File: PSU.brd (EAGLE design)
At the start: 100 x 50 mm, 20 parts, among them U1 MAX1896EUT+T

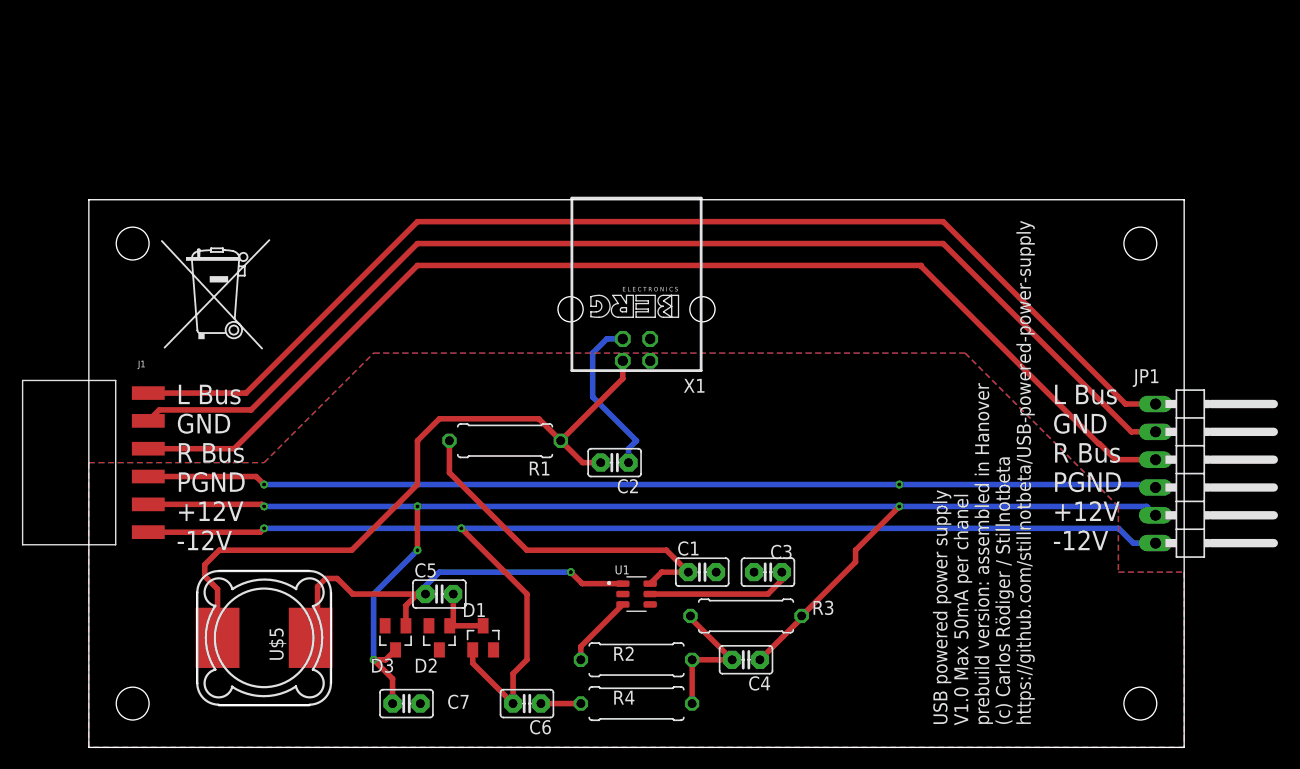
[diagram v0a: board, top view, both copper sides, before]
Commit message: V 1.1
These files have not been peer-reviewed and should NOT be manufactured.
Changes: Added rounded corners, added connection between U1 Pin 6 and Pin 4
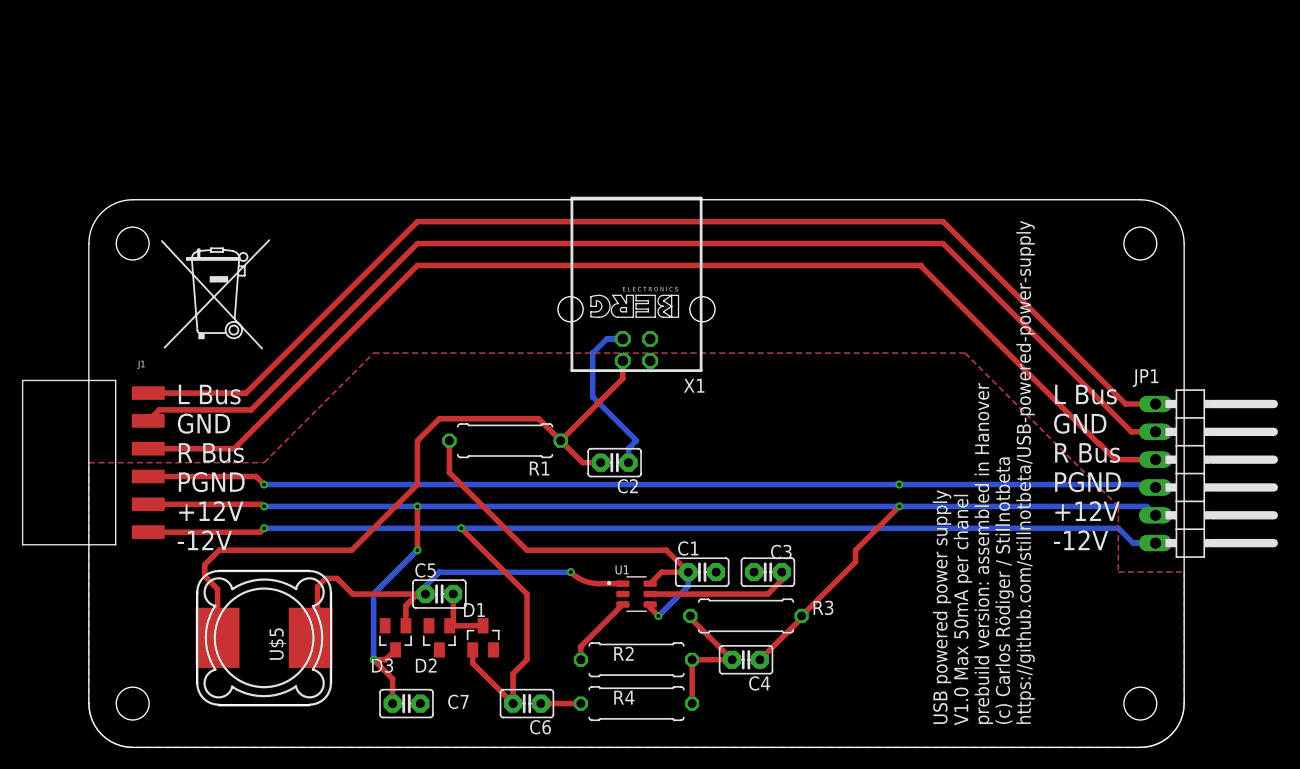
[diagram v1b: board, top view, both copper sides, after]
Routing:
- net N$1: track 32.4 -> 38.9 mm, vias 0 -> 1
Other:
- outline, holes or cut-outs redrawn
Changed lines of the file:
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@@
 <layer number="14" name="Route14" color="22" fill="1" visible="no" active="no"/>
 <layer number="15" name="Route15" color="23" fill="1" visible="no" active="no"/>
-<layer number="16" name="Bottom" color="1" fill="1" visible="no" active="yes"/>
+<layer number="16" name="Bottom" color="1" fill="1" visible="yes" active="yes"/>
 <layer number="17" name="Pads" color="2" fill="1" visible="yes" active="yes"/>
 <layer number="18" name="Vias" color="2" fill="1" visible="yes" active="yes"/>
@@
 <layer number="20" name="Dimension" color="24" fill="1" visible="yes" active="yes"/>
 <layer number="21" name="tPlace" color="7" fill="1" visible="yes" active="yes"/>
-<layer number="22" name="bPlace" color="7" fill="1" visible="no" active="yes"/>
+<layer number="22" name="bPlace" color="7" fill="1" visible="yes" active="yes"/>
 <layer number="23" name="tOrigins" color="15" fill="1" visible="yes" active="yes"/>
-<layer number="24" name="bOrigins" color="15" fill="1" visible="no" active="yes"/>
+<layer number="24" name="bOrigins" color="15" fill="1" visible="yes" active="yes"/>
 <layer number="25" name="tNames" color="7" fill="1" visible="yes" active="yes"/>
-<layer number="26" name="bNames" color="7" fill="1" visible="no" active="yes"/>
+<layer number="26" name="bNames" color="7" fill="1" visible="yes" active="yes"/>
 <layer number="27" name="tValues" color="7" fill="1" visible="no" active="yes"/>
 <layer number="28" name="bValues" color="7" fill="1" visible="no" active="yes"/>
@@
 <layer number="38" name="bTest" color="7" fill="1" visible="no" active="yes"/>
 <layer number="39" name="tKeepout" color="4" fill="11" visible="yes" active="yes"/>
-<layer number="40" name="bKeepout" color="1" fill="11" visible="no" active="yes"/>
+<layer number="40" name="bKeepout" color="1" fill="11" visible="yes" active="yes"/>
 <layer number="41" name="tRestrict" color="4" fill="10" visible="yes" active="yes"/>
-<layer number="42" name="bRestrict" color="1" fill="10" visible="no" active="yes"/>
+<layer number="42" name="bRestrict" color="1" fill="10" visible="yes" active="yes"/>
 <layer number="43" name="vRestrict" color="2" fill="10" visible="no" active="yes"/>
 <layer number="44" name="Drills" color="7" fill="1" visible="no" active="yes"/>
@@
 <layer number="50" name="dxf" color="7" fill="1" visible="no" active="no"/>
 <layer number="51" name="tDocu" color="7" fill="1" visible="yes" active="yes"/>
-<layer number="52" name="bDocu" color="7" fill="1" visible="no" active="yes"/>
+<layer number="52" name="bDocu" color="7" fill="1" visible="yes" active="yes"/>
 <layer number="53" name="tGND_GNDA" color="7" fill="9" visible="no" active="no"/>
 <layer number="54" name="bGND_GNDA" color="1" fill="9" visible="no" active="no"/>
@@
 <layer number="116" name="Patch_BOT" color="9" fill="4" visible="no" active="yes"/>
 <layer number="118" name="Rect_Pads" color="7" fill="1" visible="no" active="no"/>
-<layer number="121" name="_tsilk" color="7" fill="1" visible="yes" active="yes"/>
+<layer number="121" name="_tsilk" color="7" fill="1" visible="no" active="yes"/>
 <layer number="122" name="_bsilk" color="7" fill="1" visible="no" active="yes"/>
 <layer number="123" name="tTestmark" color="7" fill="1" visible="no" active="yes"/>
@@
 <fusionsync huburn="a.cGVyc29uYWw6dWUyYmE3ZDZl" projecturn="a.cGVyc29uYWw6dWUyYmE3ZDZlIzIwMTcwNTA1NzQ4NTIyODE" f3durn="urn:adsk.wipprod:dm.lineage:uawfAnelRH2on2N3GdXk7w" pcbguid="aad5af53-3583-4add-b30d-1d9b4c1b4db2" lastpulledtime="" lastsyncedchangeguid="534e6288-a7c1-ac99-14e8-bf617d38bbd9"/>
 <plain>
-<wire x1="0" y1="0" x2="100" y2="0" width="0" layer="20"/>
-<wire x1="100" y1="0" x2="100" y2="50" width="0" layer="20"/>
-<wire x1="100" y1="50" x2="0" y2="50" width="0" layer="20"/>
-<wire x1="0" y1="50" x2="0" y2="0" width="0" layer="20"/>
+<wire x1="0" y1="46" x2="0" y2="4" width="0" layer="20"/>
+<wire x1="0" y1="4" x2="4" y2="0" width="0" layer="20" curve="90"/>
+<wire x1="4" y1="0" x2="96" y2="0" width="0" layer="20"/>
+<wire x1="96" y1="0" x2="100" y2="4" width="0" layer="20" curve="90"/>
+<wire x1="100" y1="4" x2="100" y2="46" width="0" layer="20"/>
+<wire x1="100" y1="46" x2="96" y2="50" width="0" layer="20" curve="90"/>
+<wire x1="96" y1="50" x2="4" y2="50" width="0" layer="20"/>
+<wire x1="4" y1="50" x2="0" y2="46" width="0" layer="20" curve="90"/>
 <hole x="4" y="4" drill="3"/>
 <hole x="4" y="46" drill="3"/>
@@
 +12V
 -12V</text>
-<text x="86" y="2" size="1.27" layer="112" rot="R90">USB powered power supply
+<text x="86" y="2" size="1.27" layer="121" rot="R90">USB powered power supply
 V1.0 Max 50mA per chanel
 prebuild version: assembled in Hanover
@@
 <wire x1="40" y1="18" x2="32.92" y2="25.08" width="0.508" layer="1"/>
 <wire x1="32.92" y1="25.08" x2="32.92" y2="28" width="0.508" layer="1"/>
-<wire x1="51.245" y1="14.95" x2="51.245" y2="13.05" width="0" layer="19" extent="1-1"/>
+<wire x1="51.245" y1="13.05" x2="51.245" y2="12.755" width="0.508" layer="1"/>
+<wire x1="51.245" y1="12.755" x2="52" y2="12" width="0.508" layer="1"/>
+<via x="52" y="12" extent="1-16" drill="0.35"/>
+<wire x1="52" y1="12" x2="54.73" y2="14.73" width="0.508" layer="16"/>
+<wire x1="54.73" y1="14.73" x2="54.73" y2="16" width="0.508" layer="16"/>
 </signal>
 <signal name="N$2">
 <contactref element="R2" pad="2"/>
 <contactref element="R3" pad="1"/>
-<contactref element="R4" pad="2"/>
 <contactref element="R4" pad="2"/>
 <contactref element="C4" pad="2"/>
@@
 <wire x1="32" y1="16" x2="44" y2="16" width="0.508" layer="16"/>
 <via x="44" y="16" extent="1-16" drill="0.35"/>
-<wire x1="44" y1="16" x2="45.05" y2="14.95" width="0.508" layer="1"/>
-<wire x1="45.05" y1="14.95" x2="48.755" y2="14.95" width="0.508" layer="1"/>
+<wire x1="44" y1="16" x2="46.534925" y2="14.95" width="0.508" layer="1" curve="45"/>
+<wire x1="46.534925" y1="14.95" x2="48.755" y2="14.95" width="0.508" layer="1"/>
 </signal>
 <signal name="N$7">
@@
 <vertex x="94" y="16"/>
 <vertex x="100" y="16"/>
-<vertex x="100" y="0"/>
-<vertex x="0" y="0"/>
+<vertex x="100" y="4" curve="-90"/>
+<vertex x="96" y="0"/>
+<vertex x="4" y="0" curve="-90"/>
+<vertex x="0" y="4"/>
 </polygon>
 <polygon width="0.508" layer="16">
@@
 <vertex x="94" y="16"/>
 <vertex x="100" y="16"/>
-<vertex x="100" y="0"/>
-<vertex x="0" y="0"/>
+<vertex x="100" y="4" curve="-90"/>
+<vertex x="96" y="0"/>
+<vertex x="4" y="0" curve="-90"/>
+<vertex x="0" y="4"/>
 </polygon>
 <contactref element="X1" pad="4"/>
@@
 <contactref element="J1" pad="6"/>
 <wire x1="5.425" y1="32.35" x2="14.35" y2="32.35" width="0.508" layer="1"/>
-<wire x1="30" y1="48" x2="78" y2="48" width="0.508" layer="1"/>
-<wire x1="14.35" y1="32.35" x2="30" y2="48" width="0.508" layer="1"/>
+<wire x1="78" y1="48" x2="30" y2="48" width="0.508" layer="1"/>
+<wire x1="30" y1="48" x2="14.35" y2="32.35" width="0.508" layer="1"/>
 <wire x1="97.39" y1="31.35" x2="94.65" y2="31.35" width="0.508" layer="1"/>
 <wire x1="94.65" y1="31.35" x2="78" y2="48" width="0.508" layer="1"/>
@@
 </signals>
 <mfgpreviewcolors>
-<mfgpreviewcolor name="soldermaskcolor" color="0xC8008000"/>
-<mfgpreviewcolor name="silkscreencolor" color="0xFFFEFEFE"/>
-<mfgpreviewcolor name="backgroundcolor" color="0xFF282828"/>
+<mfgpreviewcolor name="soldermaskcolor" color="0xC8000000"/>
+<mfgpreviewcolor name="silkscreencolor" color="0xFFFFFFFF"/>
+<mfgpreviewcolor name="backgroundcolor" color="0xFFFFFFFF"/>
 <mfgpreviewcolor name="coppercolor" color="0xFFFFBF00"/>
 <mfgpreviewcolor name="substratecolor" color="0xFF786E46"/>

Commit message: V 1.1
The first iteration of the PSU, we don't recommend to put these into production until they have been tested.
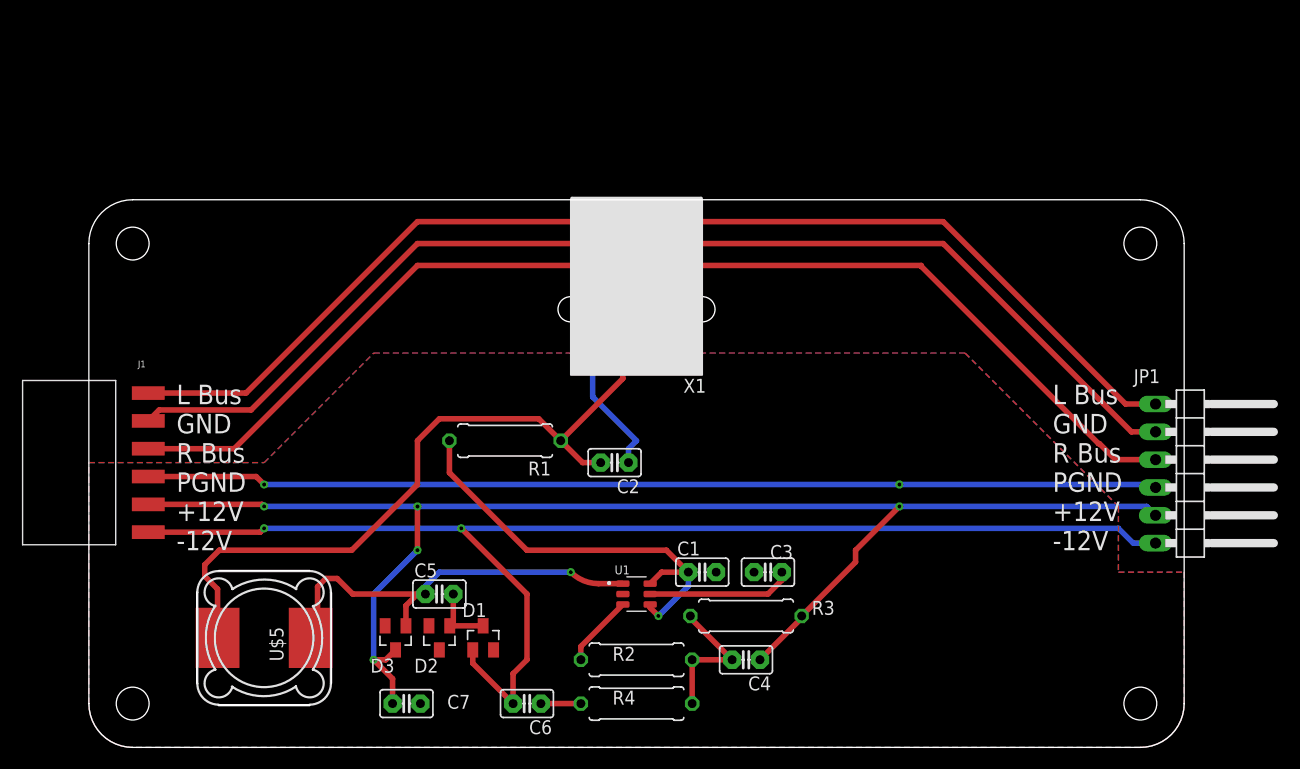
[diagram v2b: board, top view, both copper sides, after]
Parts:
- removed U$6: (no value), logo:MUELLTONNE_10.00
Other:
- board text added: "(c) Carlos Rödiger / Stillnotbeta prebuild version: assembled in Hanover Max 50mA per chanel"
- board text added: "Stillnotbeta modular mixer USB powered power supply V1.1 https://github.com/stillnotbeta/modular-mixer-psu-usb"
- board text removed: "USB powered power supply V1.0 Max 50mA per chanel prebuild version: assembled in Hanover (c) Carlos Rödiger / Stillnotbeta https://github.com/stillnotbeta/USB-powered-power-supply"
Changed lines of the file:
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@@
 <drawing>
 <settings>
-<setting alwaysvectorfont="yes"/>
+<setting alwaysvectorfont="no"/>
 <setting verticaltext="up"/>
 </settings>
@@
 <layer number="116" name="Patch_BOT" color="9" fill="4" visible="no" active="yes"/>
 <layer number="118" name="Rect_Pads" color="7" fill="1" visible="no" active="no"/>
-<layer number="121" name="_tsilk" color="7" fill="1" visible="no" active="yes"/>
-<layer number="122" name="_bsilk" color="7" fill="1" visible="no" active="yes"/>
+<layer number="121" name="_tsilk" color="7" fill="1" visible="yes" active="yes"/>
+<layer number="122" name="_bsilk" color="7" fill="1" visible="yes" active="yes"/>
 <layer number="123" name="tTestmark" color="7" fill="1" visible="no" active="yes"/>
 <layer number="124" name="bTestmark" color="7" fill="1" visible="no" active="yes"/>
@@
 +12V
 -12V</text>
-<text x="86" y="2" size="1.27" layer="121" rot="R90">USB powered power supply
-V1.0 Max 50mA per chanel
+<text x="92" y="32" size="1.778" layer="122" rot="MR0">Stillnotbeta modular mixer
+USB powered power supply V1.1
+https://github.com/stillnotbeta/modular-mixer-psu-usb</text>
+<text x="14" y="48" size="1.778" layer="122" rot="MR270">(c) Carlos Rödiger / Stillnotbeta
 prebuild version: assembled in Hanover
-(c) Carlos Rödiger / Stillnotbeta
-https://github.com/stillnotbeta/USB-powered-power-supply</text>
+Max 50mA per chanel
+</text>
+<polygon width="0.1524" layer="121">
+<vertex x="44" y="50"/>
+<vertex x="56" y="50"/>
+<vertex x="56" y="34"/>
+<vertex x="44" y="34"/>
+</polygon>
 </plain>
 <attributes>
@@
 <attribute name="VALUE" x="42.38" y="48.89" size="1.27" layer="27" rot="R270"/>
 </element>
-<element name="U$6" library="logo" library_urn="urn:adsk.eagle:library:264" package="MUELLTONNE_10.00" value="" x="6" y="36" smashed="yes"/>
 </elements>
 <signals>
